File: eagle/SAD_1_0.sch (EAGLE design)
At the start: 14 parts, among them X1 A, X2 B, X3 C, X4 D, X5 E, X6 F

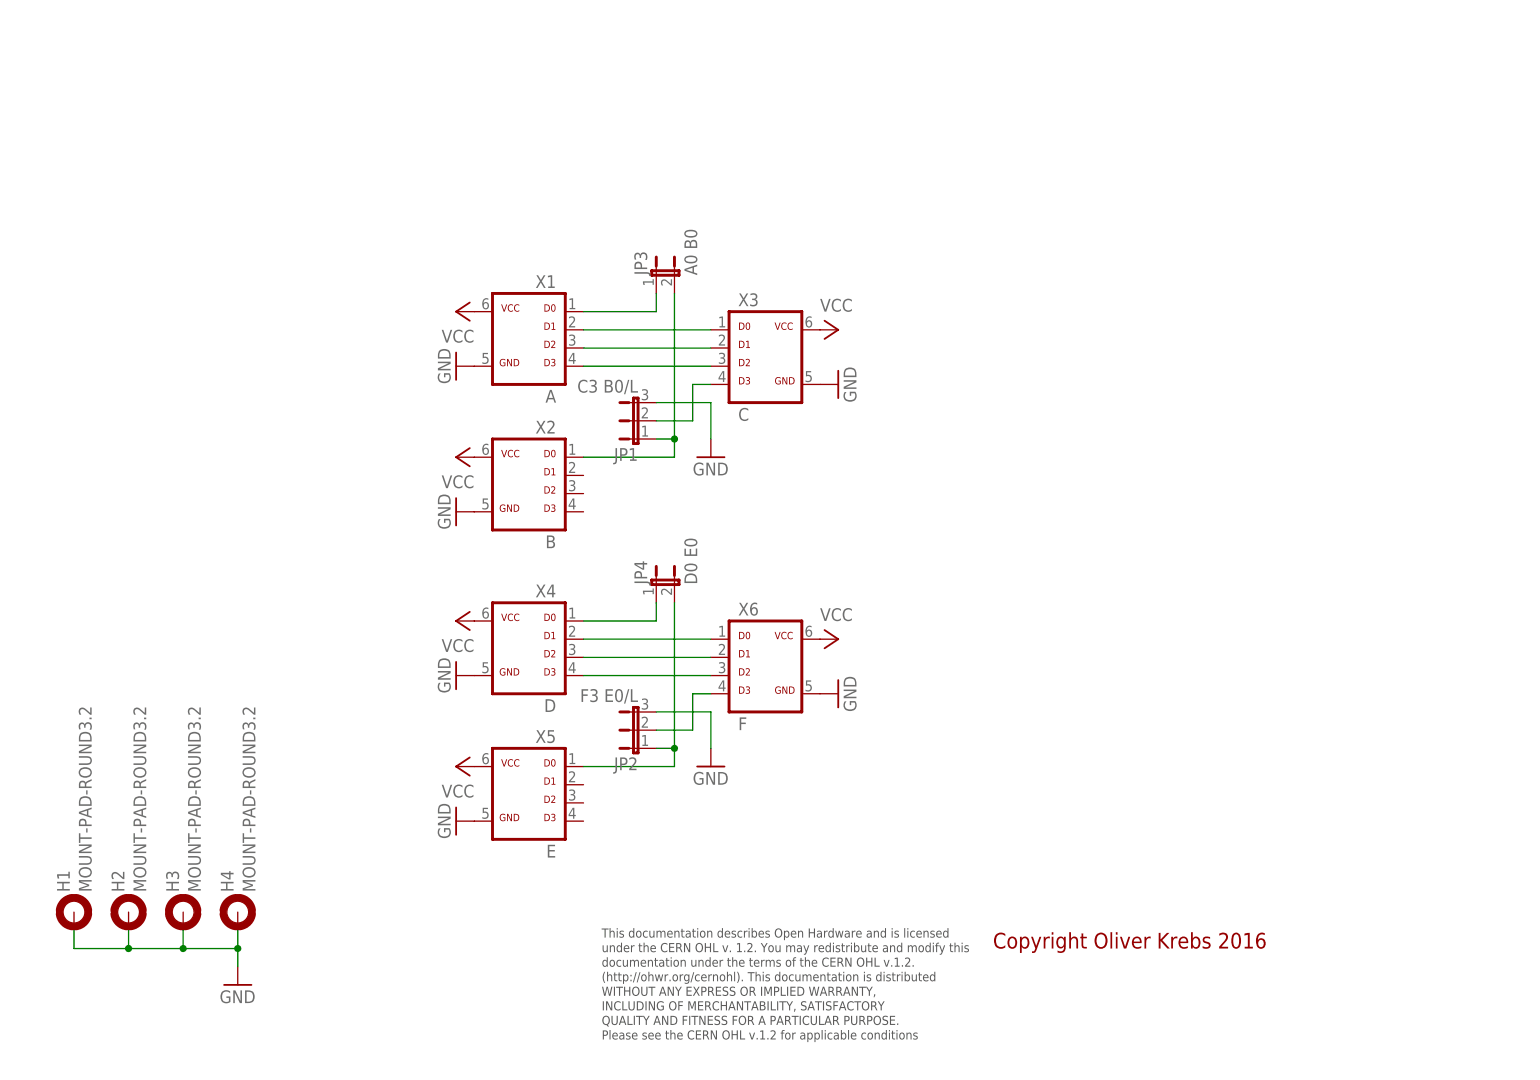
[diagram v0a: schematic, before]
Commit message: Add new tetra-Board and arduino files
Add AMP_1_0, AVC_1_0, D18_1_1, IOP_1_2, MIC_1_0, PIN_1_1, POT_1_0, PWA_1_0, PWR_1_0, RGF 2.0, SOC_2_0, VLT_1_0
Add mex_nano_shield_keyboard, mex_nano_shied_numbers

New arduino projects
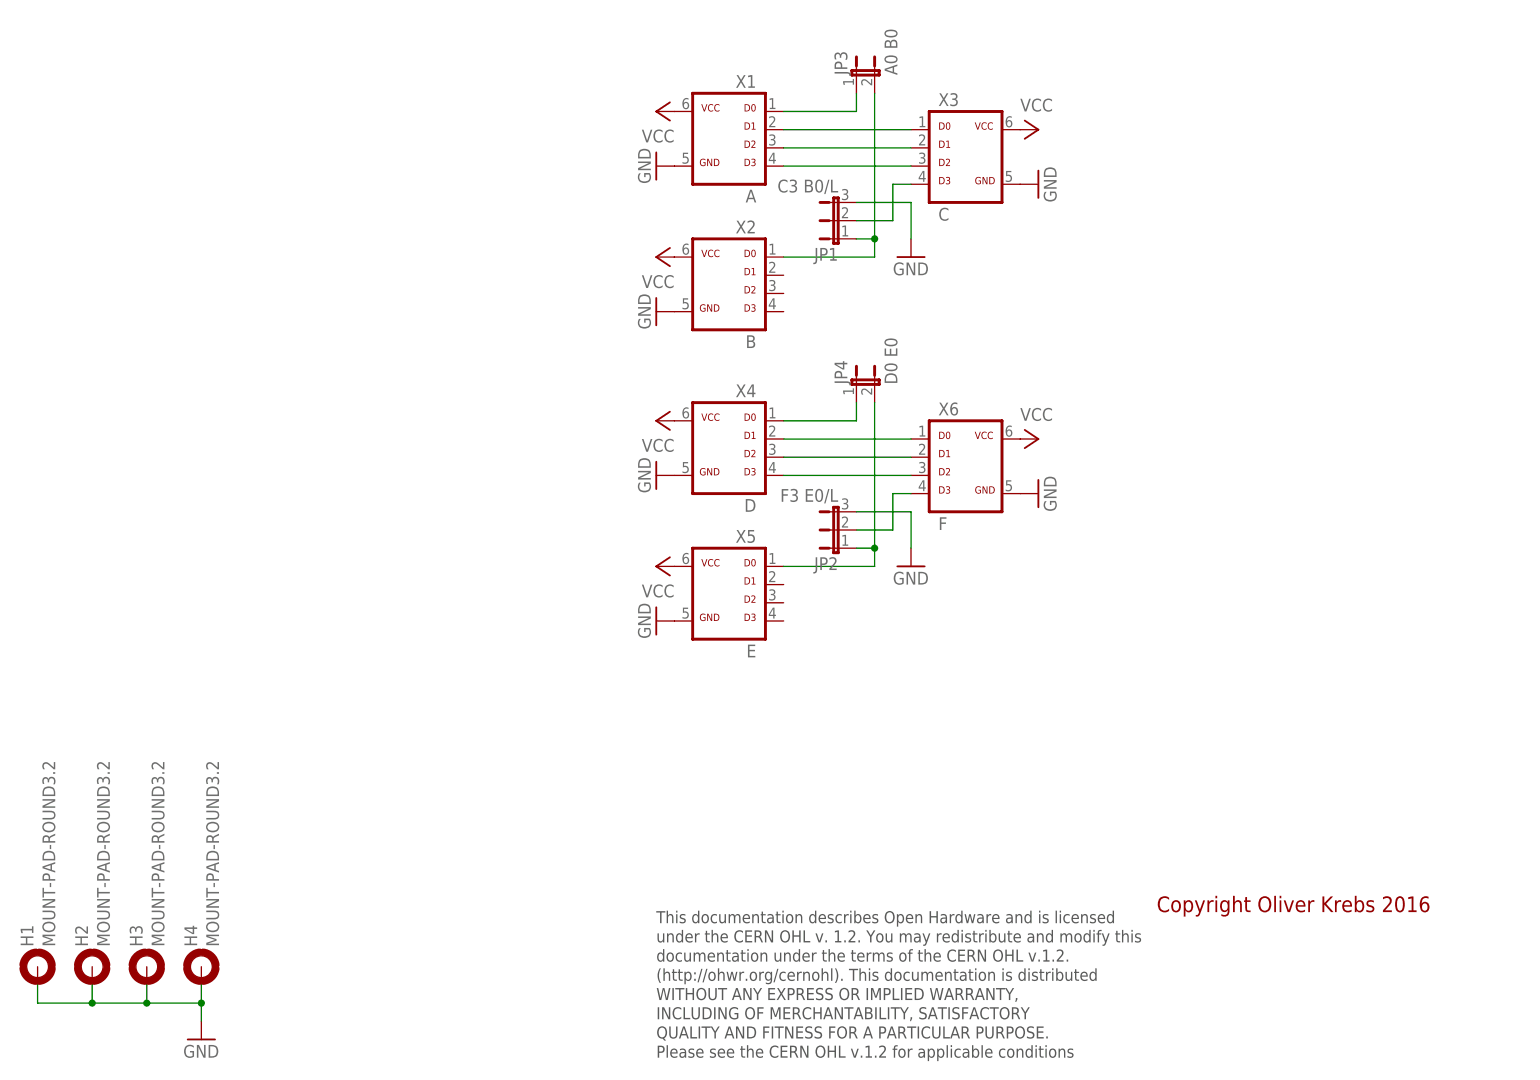
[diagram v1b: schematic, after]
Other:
- moved on the sheet: H1, H2, H3, H4, JP1, JP2, JP3, JP4, X1, X2, X3, X4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
